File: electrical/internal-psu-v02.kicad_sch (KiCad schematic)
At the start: 15 parts, among them J201 T1 SEC 1, J202 T1 SEC 2, J203 TO AMP J5

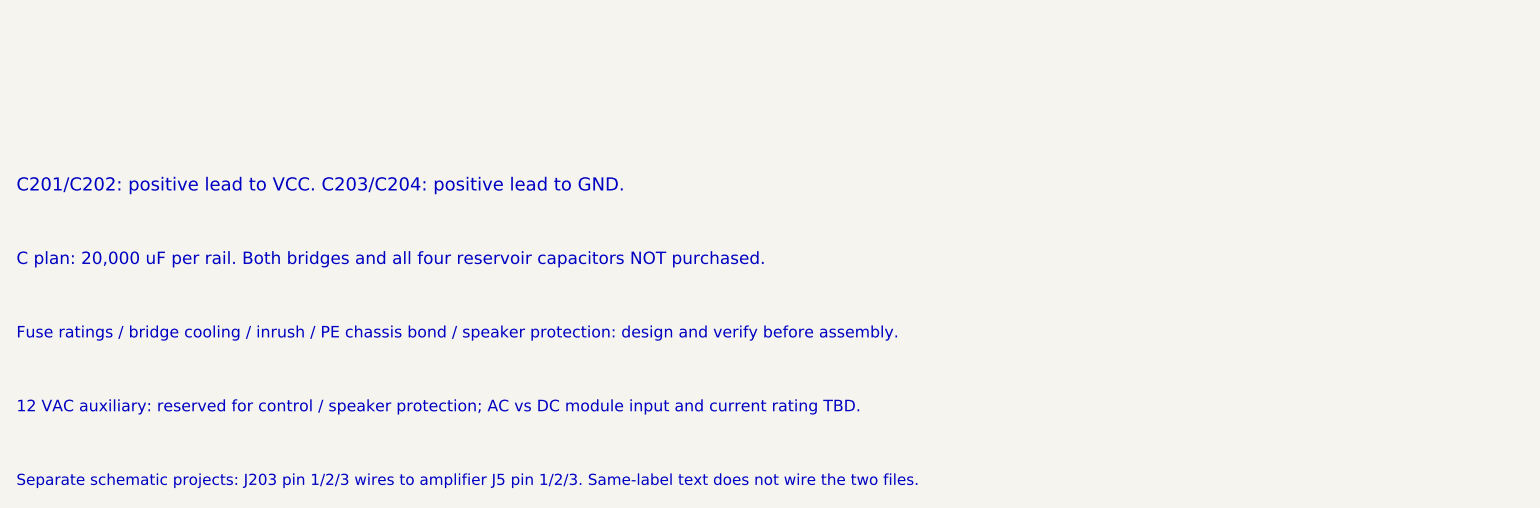
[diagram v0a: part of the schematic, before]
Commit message: rebuild: 原理圖與 PCB 以本機 KiCad 10.0.6 重建，兩板 DRC 0 違規
- 原理圖：ERC 0；verify_electrical 期望值改為實購 100V／0.6W 後通過
- PCB：修正首輪 DRC（C2/R1 保留區重疊、U1 絲印字高與壓字）與回地分組碰觸
  （靜音回流改經 via_mute_ret），DRC 0 違規 0 未連通，verify/analyze/test 通過
- 工具：KiCad 在 Windows 寫出的 CRLF 轉 LF 後才雜湊；雜湊路徑改 as_posix()
- 文件同步；pcb/inspection-v03 與 docs/diagrams 尚未重建

Co-Authored-By: Claude Opus 5.5 (1M context) <noreply@anthropic.com>
Claude-Session: https://claude.ai/code/session_01DerP5HjoiFxZ4hz4f3ygqt
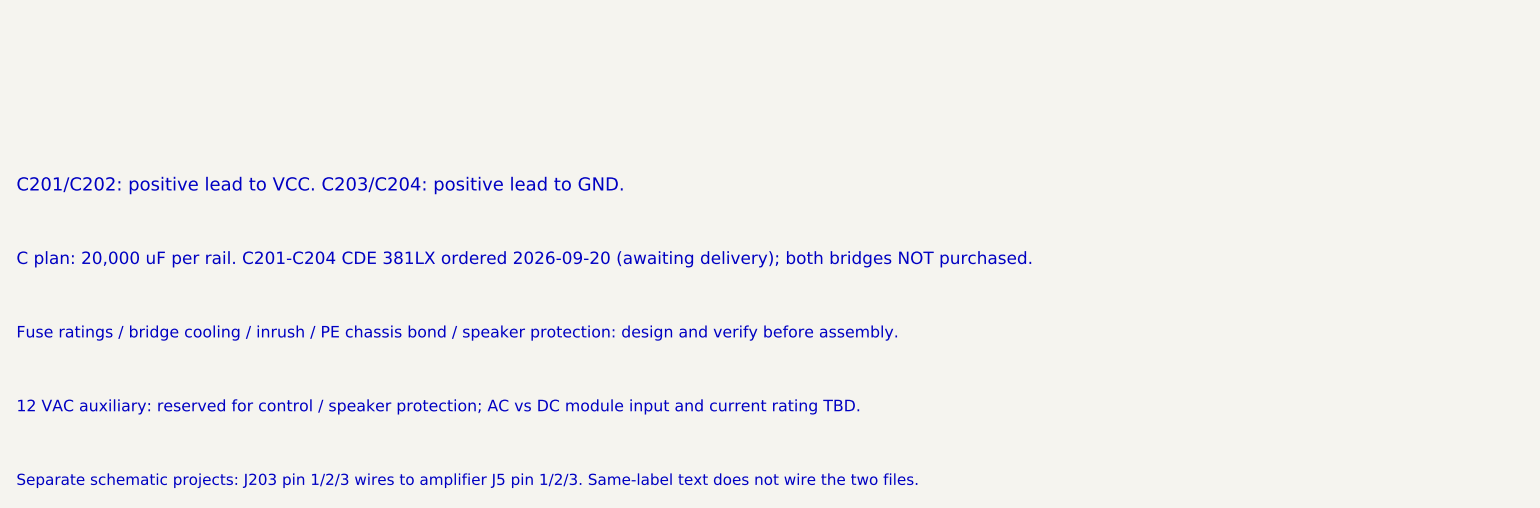
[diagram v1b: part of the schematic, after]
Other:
- note added: "C plan: 20,000 uF per rail. C201-C204 CDE 381LX ordered 2026-09-20 (awaiting delivery); both bridges NOT purchased."
- note removed: "C plan: 20,000 uF per rail. Both bridges and all four reservoir capacitors NOT purchased."

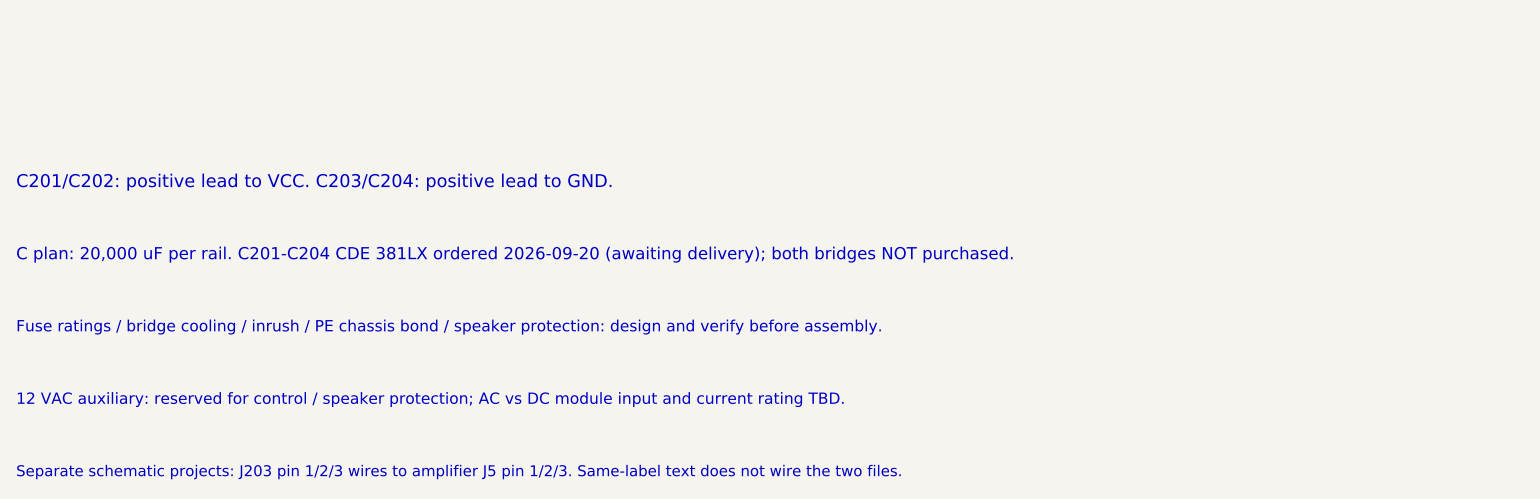
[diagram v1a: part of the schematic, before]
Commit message: docs/preview: 複核後修正過期字樣、C2 距離與機殼寬度註記；重建電源圖並重綁雜湊
Co-Authored-By: Claude Fable 5.1 <noreply@anthropic.com>
Claude-Session: https://claude.ai/code/session_01DerP5HjoiFxZ4hz4f3ygqt
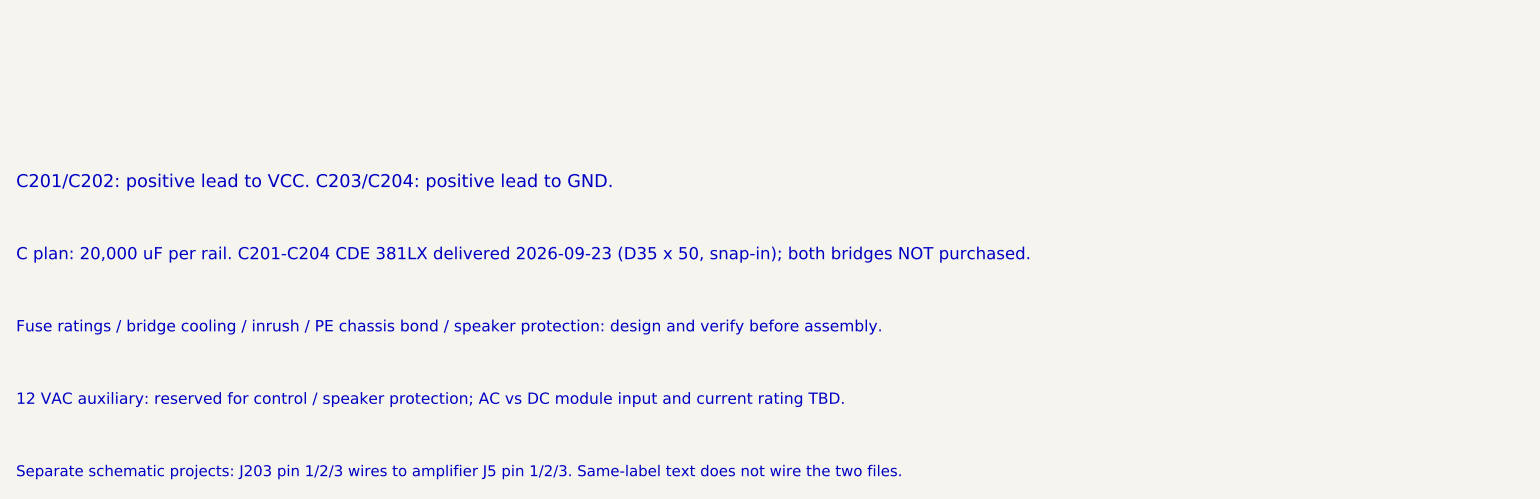
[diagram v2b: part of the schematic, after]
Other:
- note added: "C plan: 20,000 uF per rail. C201-C204 CDE 381LX delivered 2026-09-23 (D35 x 50, snap-in); both bridges NOT purchased."
- note removed: "C plan: 20,000 uF per rail. C201-C204 CDE 381LX ordered 2026-09-20 (awaiting delivery); both bridges NOT purchased."

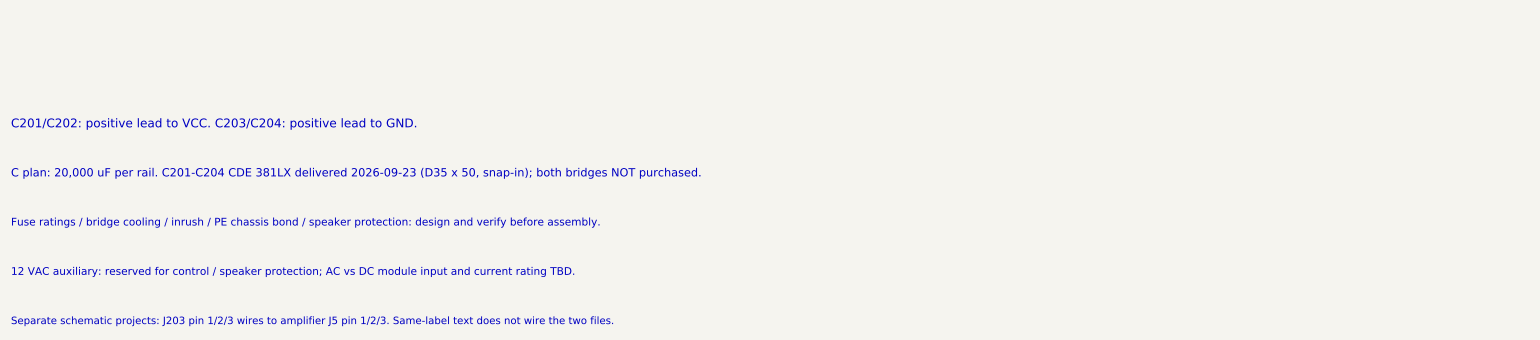
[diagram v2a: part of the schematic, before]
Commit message: pcb: 整流橋定案鎖機殼（方案 A），電源板改 4 位端子並重建，DRC 0
- BridgeTerminal4_P5.08 取代 Bridge_LOGICAL_UNVERIFIED（焊盤編號沿用 AC1/AC2/P/N）
- BR1/BR2 轉 270°，四條 4 mm 進出線加轉折避開相鄰端子
- 電源圖註記、採購總表（§1.1／§2.1，新增 Faston 端子與線材）、HANDOFF、pcb/README、CHANGELOG、README 同步
- 兩板 DRC 0 違規 0 未連通；verify_electrical／power_supply／pcb、analyze、單元測試通過

Co-Authored-By: Claude Fable 5.1 <noreply@anthropic.com>
Claude-Session: https://claude.ai/code/session_01DerP5HjoiFxZ4hz4f3ygqt
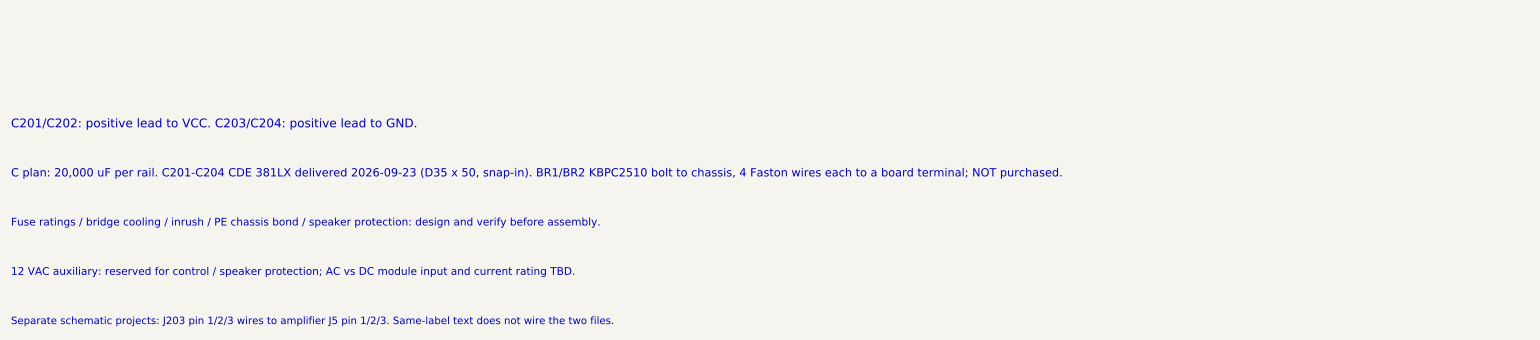
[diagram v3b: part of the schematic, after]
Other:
- note added: "C plan: 20,000 uF per rail. C201-C204 CDE 381LX delivered 2026-09-23 (D35 x 50, snap-in). BR1/BR2 KBPC2510 bolt to chassis, 4 Faston wires each to a board terminal; NOT purchased."
- note removed: "C plan: 20,000 uF per rail. C201-C204 CDE 381LX delivered 2026-09-23 (D35 x 50, snap-in); both bridges NOT purchased."

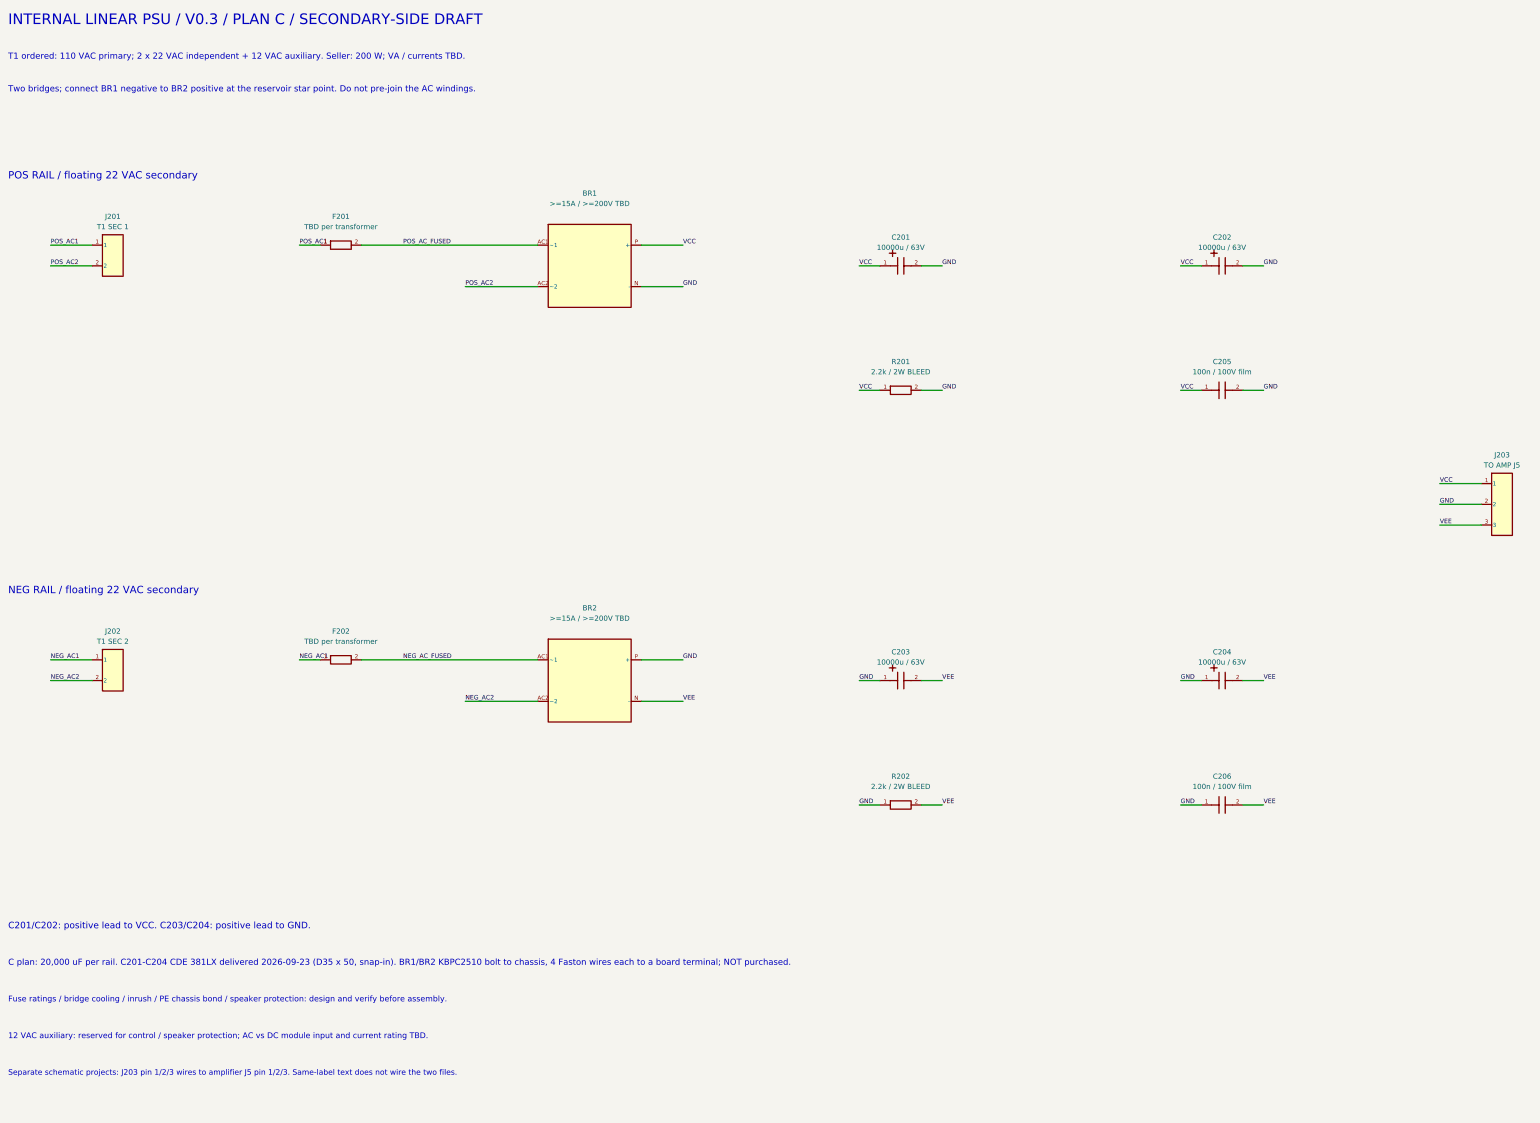
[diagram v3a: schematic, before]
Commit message: psu: V0.4 原理圖加第二組輸出端子 J204 與每繞組 snubber 預留位（僅原理圖，PCB 未畫）
- J203 給左聲道、J204 給右聲道，各自從匯流點供電，避免兩聲道共用端子與線電阻
- R203/C207/C208、R204/C209/C210 為 Cx‖(Rs+Cs) 緩衝預留位，元件值待變壓器實測後定，首次上電不裝
- verify_power_supply.py 期望值同步（22 元件、11 網路），ERC 0 違規

Co-Authored-By: Claude Fable 5.1 <noreply@anthropic.com>
Claude-Session: https://claude.ai/code/session_01DerP5HjoiFxZ4hz4f3ygqt
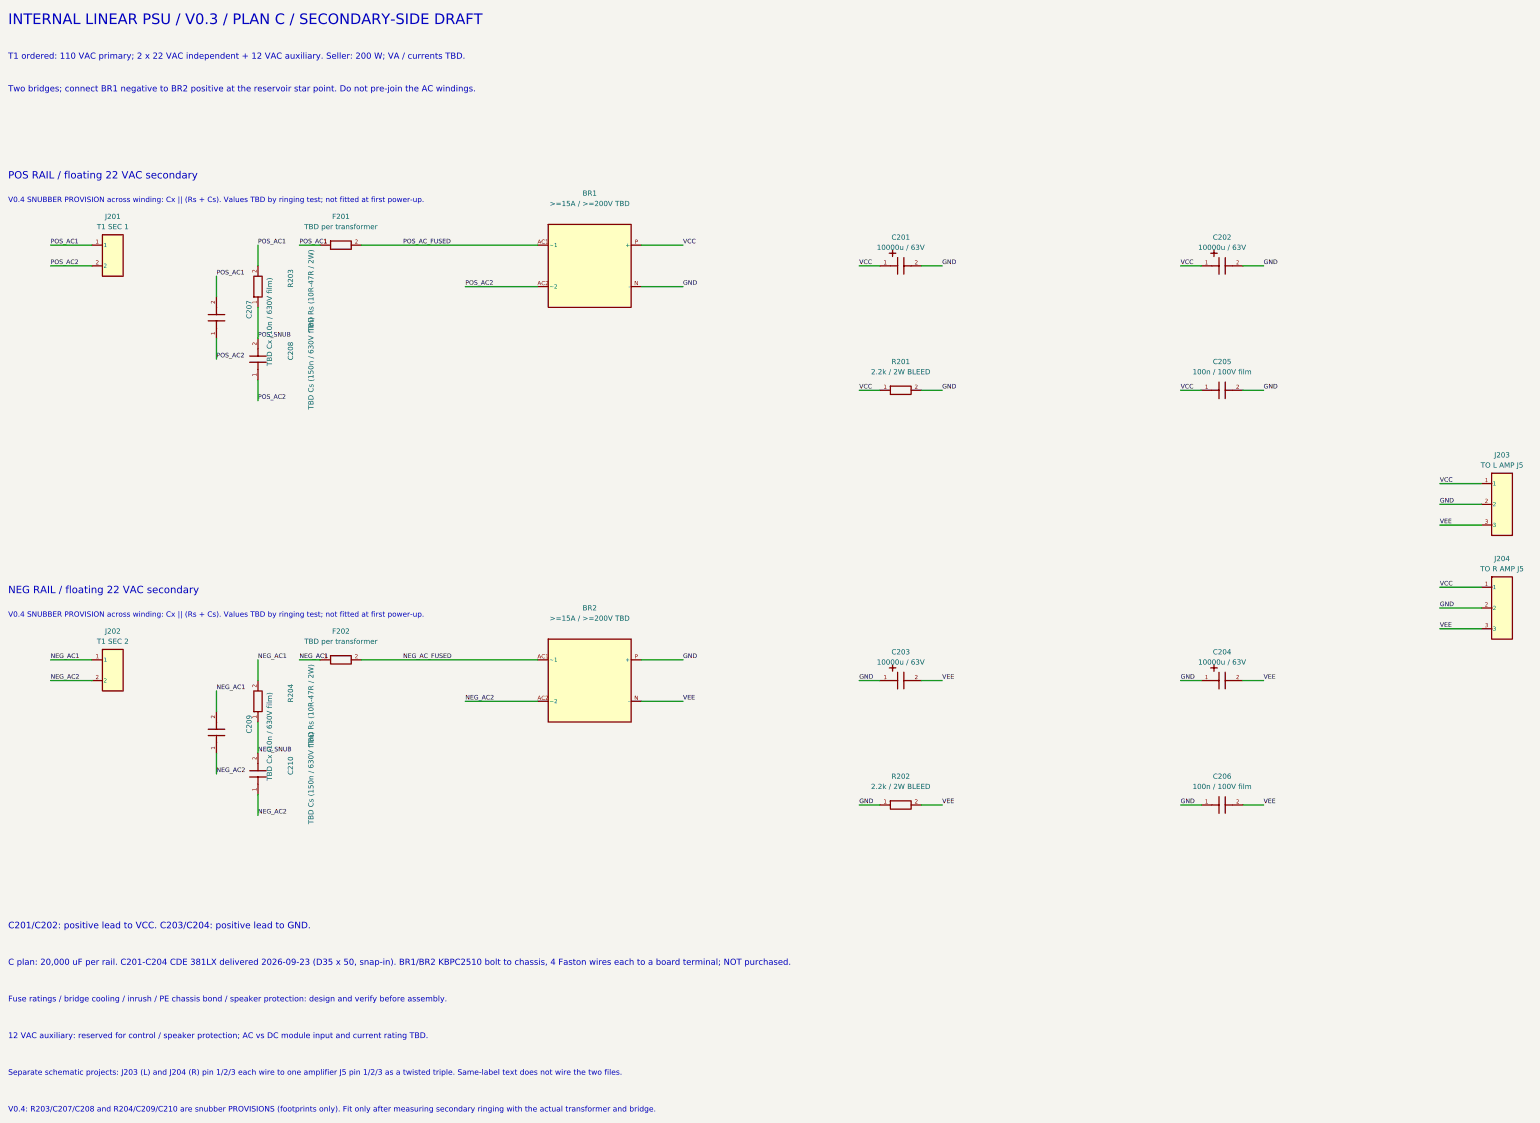
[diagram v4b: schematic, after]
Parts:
- added C207, C209: TBD Cx (10n / 630V film), symbol Project:C
- added C208, C210: TBD Cs (150n / 630V film), symbol Project:C
- added J204: TO R AMP J5, symbol Project:Conn3
- added R203, R204: TBD Rs (10R-47R / 2W), symbol Project:R
- J203: value TO AMP J5 -> TO L AMP J5
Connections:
- net GND: now also J204.2
- net NEG_AC1: now also C209.2, R204.2
- net NEG_AC2: now also C209.1, C210.1
- net POS_AC1: now also C207.2, R203.2
- net POS_AC2: now also C207.1, C208.1
- net VCC: now also J204.1
- net VEE: now also J204.3
- new net NEG_SNUB: C210.2, R204.1
- new net POS_SNUB: C208.2, R203.1
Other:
- note added: "Separate schematic projects: J203 (L) and J204 (R) pin 1/2/3 each wire to one amplifier J5 pin 1/2/3 as a twisted triple. Same-label text does not wire the two files."
- note added: "V0.4 SNUBBER PROVISION across winding: Cx || (Rs + Cs). Values TBD by ringing test; not fitted at first power-up."
- note added: "V0.4: R203/C207/C208 and R204/C209/C210 are snubber PROVISIONS (footprints only). Fit only after measuring secondary ringing with the actual transformer and bridge."
- note removed: "Separate schematic projects: J203 pin 1/2/3 wires to amplifier J5 pin 1/2/3. Same-label text does not wire the two files."
